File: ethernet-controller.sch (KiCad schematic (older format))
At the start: 33 parts, among them J1 5-2337992-8, U1 RTL8111H, Y1 ABM8G-25.000MHZ-18-D2Y-T

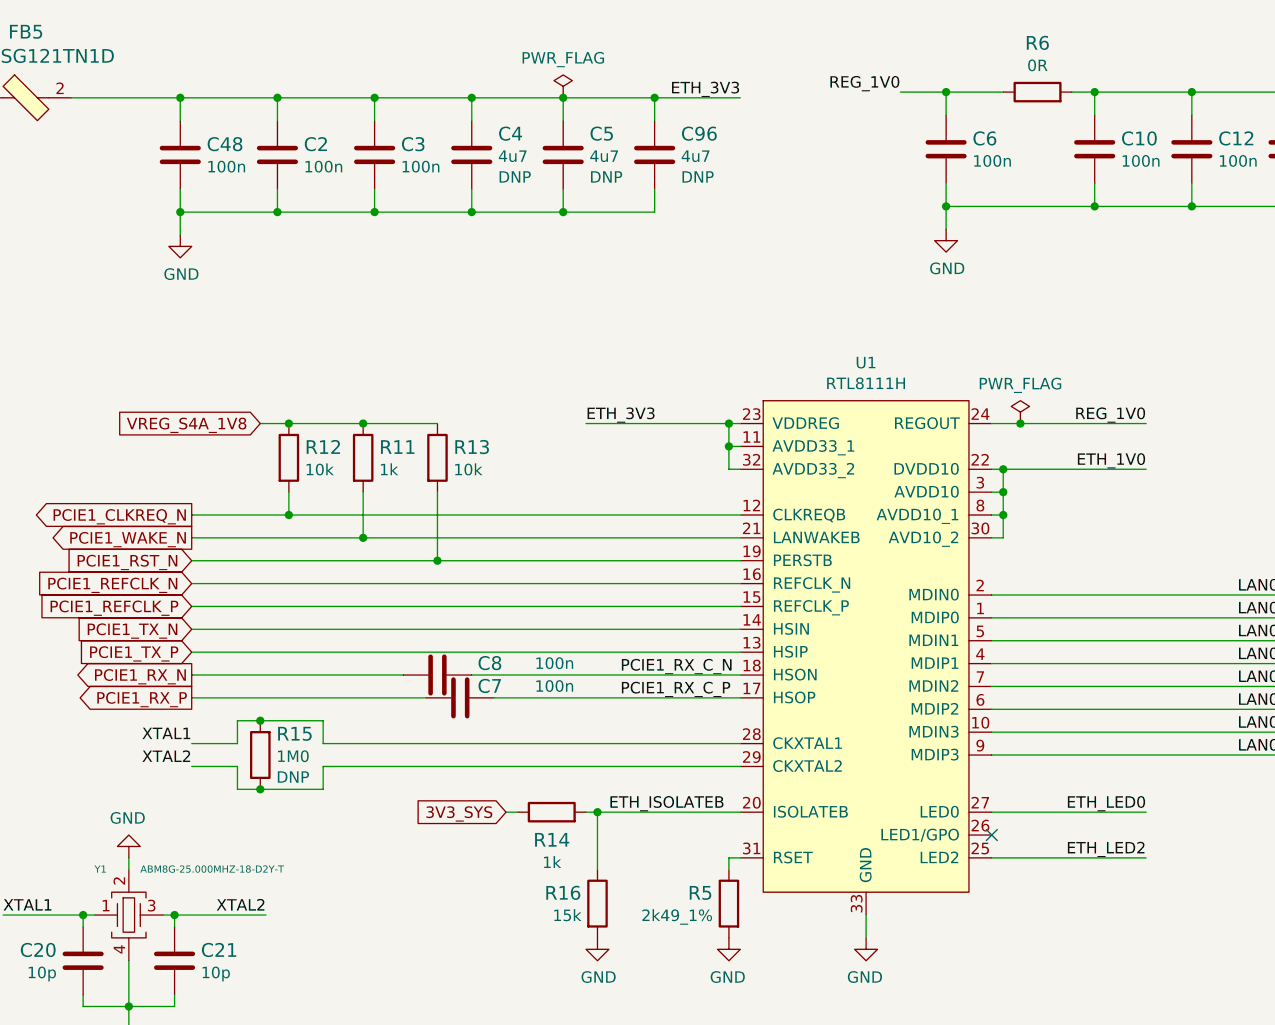
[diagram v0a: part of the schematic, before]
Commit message: Add test points
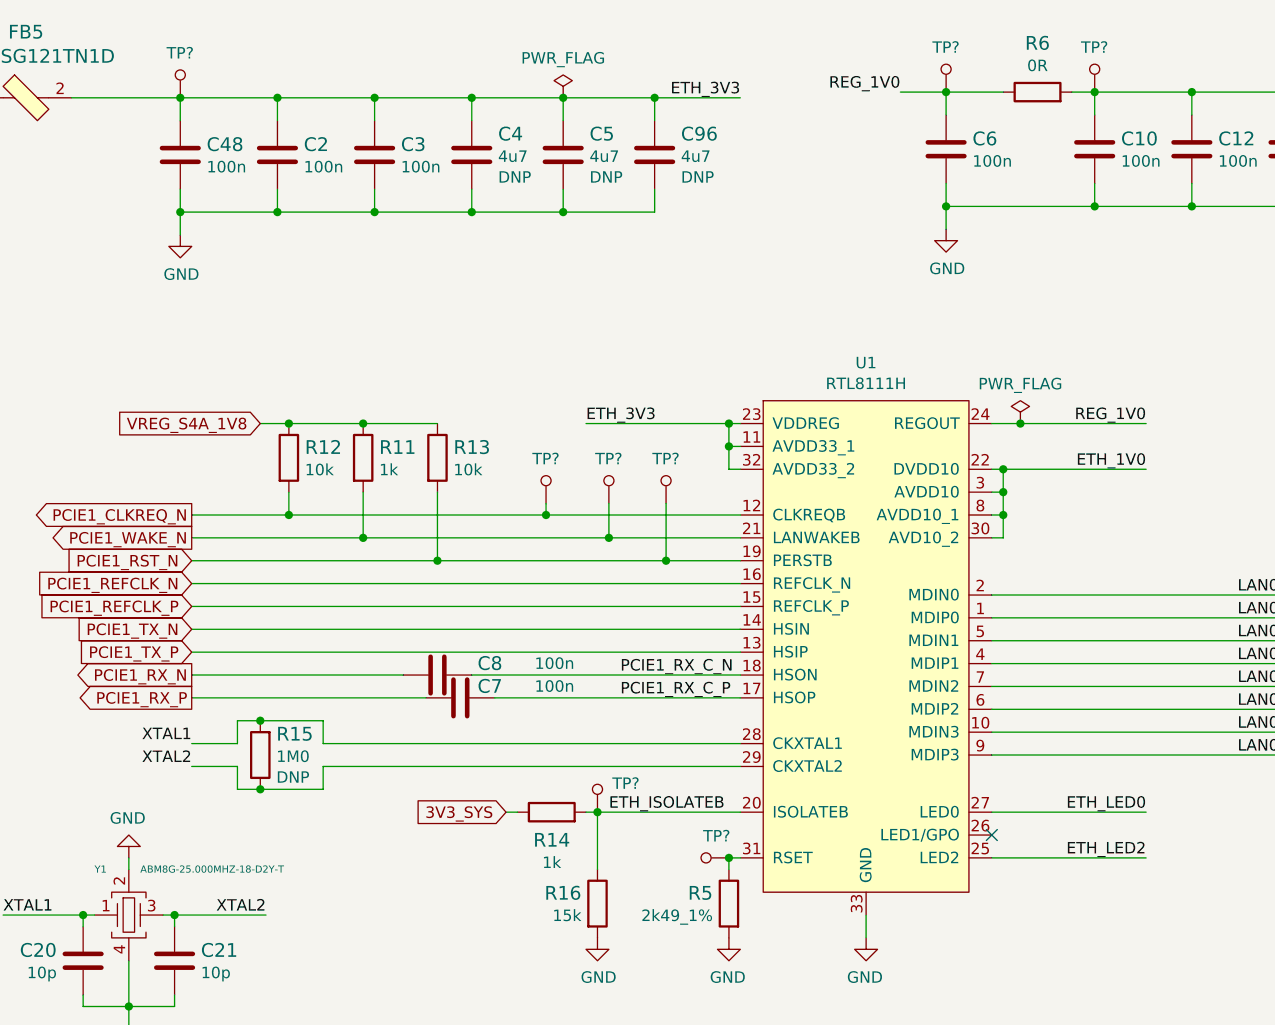
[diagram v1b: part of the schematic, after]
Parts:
- added TP? (x8): TP_SMD_0_75MM, antmicro-footprints:Testpoint_smd_0_75mm, symbol antmicroTestPoints:TP_SMD_0_75MM
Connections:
- net ETH_1V0: now also TP?.1
- net ETH_3V3: now also TP?.1
- net ETH_ISOLATEB: now also TP?.1
- net PCIE1_CLKREQ_N: now also TP?.1
- net PCIE1_RST_N: now also TP?.1
- net PCIE1_WAKE_N: now also TP?.1
- net REG_1V0: now also TP?.1
- net at R5.1, U1.31 (RSET): now also TP?.1
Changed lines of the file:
@@
 	8175 4525 8050 4525
-Wire Wire Line
-	6325 6225 6950 6225
 Wire Wire Line
 	6325 6225 6325 6475
@@
 Connection ~ 4975 4925
 Wire Wire Line
-	4975 4925 6950 4925
+	4975 4925 6100 4925
 Wire Wire Line
 	5300 4825 5300 5025
@@
 Connection ~ 5300 5025
 Wire Wire Line
-	5300 5025 6950 5025
+	5300 5025 6375 5025
 Wire Wire Line
 	5625 4825 5625 5125
 Connection ~ 5625 5125
 Wire Wire Line
-	5625 5125 6950 5125
+	5625 5125 6625 5125
 Wire Wire Line
 	4550 5225 6950 5225
@@
 Text Label 6425 5725 0    50   ~ 0
 PCIE1_RX_C_P
+$Comp
+L antmicroTestPoints:TP_SMD_0_75MM TP?
+U 1 1 624394EB
+P 4500 3000
+F 0 "TP?" H 4500 2905 50  0000 C CNN
+F 1 "TP_SMD_0_75MM" H 4500 2900 50  0001 C CNN
+F 2 "antmicro-footprints:Testpoint_smd_0_75mm" H 4700 3200 60  0001 L CNN
+F 3 "" H 4700 3300 60  0001 L CNN
+	1    4500 3000
+	-1   0    0    1
+$EndComp
+$Comp
+L antmicroTestPoints:TP_SMD_0_75MM TP?
+U 1 1 6243B4E7
+P 7850 2975
+F 0 "TP?" H 7850 2880 50  0000 C CNN
+F 1 "TP_SMD_0_75MM" H 7850 2875 50  0001 C CNN
+F 2 "antmicro-footprints:Testpoint_smd_0_75mm" H 8050 3175 60  0001 L CNN
+F 3 "" H 8050 3275 60  0001 L CNN
+	1    7850 2975
+	-1   0    0    1
+$EndComp
+$Comp
+L antmicroTestPoints:TP_SMD_0_75MM TP?
+U 1 1 62446EB7
+P 6100 4775
+F 0 "TP?" H 6100 4680 50  0000 C CNN
+F 1 "TP_SMD_0_75MM" H 6100 4675 50  0001 C CNN
+F 2 "antmicro-footprints:Testpoint_smd_0_75mm" H 6300 4975 60  0001 L CNN
+F 3 "" H 6300 5075 60  0001 L CNN
+	1    6100 4775
+	-1   0    0    1
+$EndComp
+$Comp
+L antmicroTestPoints:TP_SMD_0_75MM TP?
+U 1 1 6244F4AE
+P 6375 4775
+F 0 "TP?" H 6375 4680 50  0000 C CNN
+F 1 "TP_SMD_0_75MM" H 6375 4675 50  0001 C CNN
+F 2 "antmicro-footprints:Testpoint_smd_0_75mm" H 6575 4975 60  0001 L CNN
+F 3 "" H 6575 5075 60  0001 L CNN
+	1    6375 4775
+	-1   0    0    1
+$EndComp
+$Comp
+L antmicroTestPoints:TP_SMD_0_75MM TP?
+U 1 1 62457423
+P 6625 4775
+F 0 "TP?" H 6625 4680 50  0000 C CNN
+F 1 "TP_SMD_0_75MM" H 6625 4675 50  0001 C CNN
+F 2 "antmicro-footprints:Testpoint_smd_0_75mm" H 6825 4975 60  0001 L CNN
+F 3 "" H 6825 5075 60  0001 L CNN
+	1    6625 4775
+	-1   0    0    1
+$EndComp
+Wire Wire Line
+	6100 4875 6100 4925
+Connection ~ 6100 4925
+Wire Wire Line
+	6100 4925 6950 4925
+Wire Wire Line
+	6375 4875 6375 5025
+Connection ~ 6375 5025
+Wire Wire Line
+	6375 5025 6950 5025
+Wire Wire Line
+	6625 4875 6625 5125
+Connection ~ 6625 5125
+Wire Wire Line
+	6625 5125 6950 5125
+$Comp
+L antmicroTestPoints:TP_SMD_0_75MM TP?
+U 1 1 6247C502
+P 6325 6125
+F 0 "TP?" H 6200 6100 50  0000 C CNN
+F 1 "TP_SMD_0_75MM" H 6325 6025 50  0001 C CNN
+F 2 "antmicro-footprints:Testpoint_smd_0_75mm" H 6525 6325 60  0001 L CNN
+F 3 "" H 6525 6425 60  0001 L CNN
+	1    6325 6125
+	-1   0    0    1
+$EndComp
+Wire Wire Line
+	6325 6225 6950 6225
+$Comp
+L antmicroTestPoints:TP_SMD_0_75MM TP?
+U 1 1 6249C84E
+P 6800 6425
+F 0 "TP?" V 6705 6472 50  0000 C CNN
+F 1 "TP_SMD_0_75MM" H 6800 6325 50  0001 C CNN
+F 2 "antmicro-footprints:Testpoint_smd_0_75mm" H 7000 6625 60  0001 L CNN
+F 3 "" H 7000 6725 60  0001 L CNN
+	1    6800 6425
+	0    1    1    0
+$EndComp
+Connection ~ 6900 6425
+$Comp
+L antmicroTestPoints:TP_SMD_0_75MM TP?
+U 1 1 624AD4ED
+P 8500 2975
+F 0 "TP?" H 8500 2880 50  0000 C CNN
+F 1 "TP_SMD_0_75MM" H 8500 2875 50  0001 C CNN
+F 2 "antmicro-footprints:Testpoint_smd_0_75mm" H 8700 3175 60  0001 L CNN
+F 3 "" H 8700 3275 60  0001 L CNN
+	1    8500 2975
+	-1   0    0    1
+$EndComp
 $EndSCHEMATC

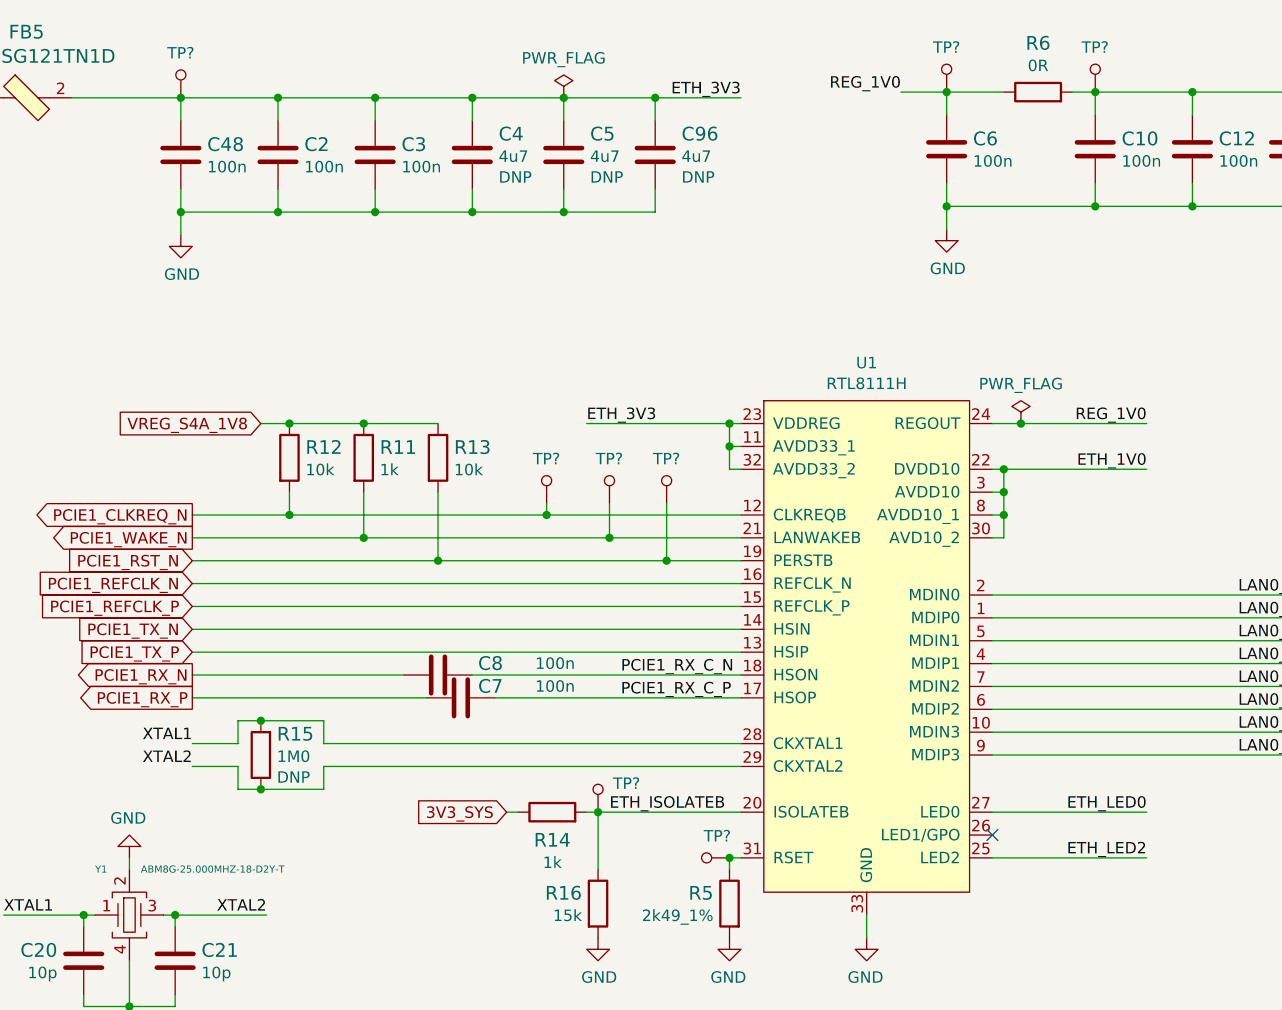
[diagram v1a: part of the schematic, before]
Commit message: Annotate test points, reimport 510R from global library
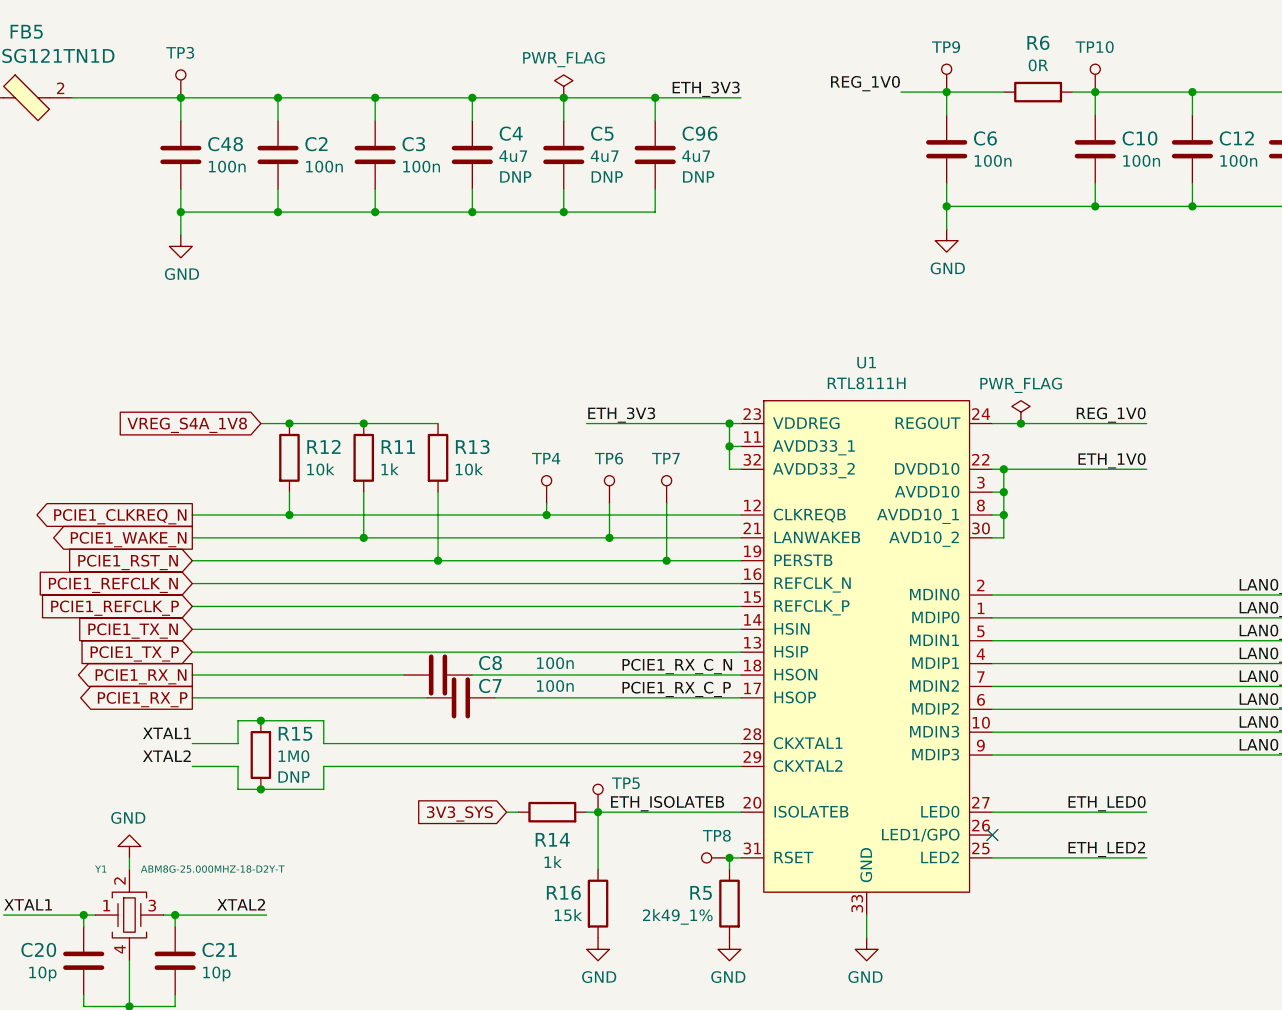
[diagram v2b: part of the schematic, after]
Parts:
- gave numbers to parts that had none: 8
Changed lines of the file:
@@
 PCIE1_RX_C_P
 $Comp
-L antmicroTestPoints:TP_SMD_0_75MM TP?
+L antmicroTestPoints:TP_SMD_0_75MM TP3
 U 1 1 624394EB
 P 4500 3000
-F 0 "TP?" H 4500 2905 50  0000 C CNN
+F 0 "TP3" H 4500 2905 50  0000 C CNN
 F 1 "TP_SMD_0_75MM" H 4500 2900 50  0001 C CNN
 F 2 "antmicro-footprints:Testpoint_smd_0_75mm" H 4700 3200 60  0001 L CNN
@@
 $EndComp
 $Comp
-L antmicroTestPoints:TP_SMD_0_75MM TP?
+L antmicroTestPoints:TP_SMD_0_75MM TP9
 U 1 1 6243B4E7
 P 7850 2975
-F 0 "TP?" H 7850 2880 50  0000 C CNN
+F 0 "TP9" H 7850 2880 50  0000 C CNN
 F 1 "TP_SMD_0_75MM" H 7850 2875 50  0001 C CNN
 F 2 "antmicro-footprints:Testpoint_smd_0_75mm" H 8050 3175 60  0001 L CNN
@@
 $EndComp
 $Comp
-L antmicroTestPoints:TP_SMD_0_75MM TP?
+L antmicroTestPoints:TP_SMD_0_75MM TP4
 U 1 1 62446EB7
 P 6100 4775
-F 0 "TP?" H 6100 4680 50  0000 C CNN
+F 0 "TP4" H 6100 4680 50  0000 C CNN
 F 1 "TP_SMD_0_75MM" H 6100 4675 50  0001 C CNN
 F 2 "antmicro-footprints:Testpoint_smd_0_75mm" H 6300 4975 60  0001 L CNN
@@
 $EndComp
 $Comp
-L antmicroTestPoints:TP_SMD_0_75MM TP?
+L antmicroTestPoints:TP_SMD_0_75MM TP6
 U 1 1 6244F4AE
 P 6375 4775
-F 0 "TP?" H 6375 4680 50  0000 C CNN
+F 0 "TP6" H 6375 4680 50  0000 C CNN
 F 1 "TP_SMD_0_75MM" H 6375 4675 50  0001 C CNN
 F 2 "antmicro-footprints:Testpoint_smd_0_75mm" H 6575 4975 60  0001 L CNN
@@
 $EndComp
 $Comp
-L antmicroTestPoints:TP_SMD_0_75MM TP?
+L antmicroTestPoints:TP_SMD_0_75MM TP7
 U 1 1 62457423
 P 6625 4775
-F 0 "TP?" H 6625 4680 50  0000 C CNN
+F 0 "TP7" H 6625 4680 50  0000 C CNN
 F 1 "TP_SMD_0_75MM" H 6625 4675 50  0001 C CNN
 F 2 "antmicro-footprints:Testpoint_smd_0_75mm" H 6825 4975 60  0001 L CNN
@@
 	6625 5125 6950 5125
 $Comp
-L antmicroTestPoints:TP_SMD_0_75MM TP?
+L antmicroTestPoints:TP_SMD_0_75MM TP5
 U 1 1 6247C502
 P 6325 6125
-F 0 "TP?" H 6200 6100 50  0000 C CNN
+F 0 "TP5" H 6200 6100 50  0000 C CNN
 F 1 "TP_SMD_0_75MM" H 6325 6025 50  0001 C CNN
 F 2 "antmicro-footprints:Testpoint_smd_0_75mm" H 6525 6325 60  0001 L CNN
@@
 	6325 6225 6950 6225
 $Comp
-L antmicroTestPoints:TP_SMD_0_75MM TP?
+L antmicroTestPoints:TP_SMD_0_75MM TP8
 U 1 1 6249C84E
 P 6800 6425
-F 0 "TP?" V 6705 6472 50  0000 C CNN
+F 0 "TP8" V 6705 6472 50  0000 C CNN
 F 1 "TP_SMD_0_75MM" H 6800 6325 50  0001 C CNN
 F 2 "antmicro-footprints:Testpoint_smd_0_75mm" H 7000 6625 60  0001 L CNN
@@
 Connection ~ 6900 6425
 $Comp
-L antmicroTestPoints:TP_SMD_0_75MM TP?
+L antmicroTestPoints:TP_SMD_0_75MM TP10
 U 1 1 624AD4ED
 P 8500 2975
-F 0 "TP?" H 8500 2880 50  0000 C CNN
+F 0 "TP10" H 8500 2880 50  0000 C CNN
 F 1 "TP_SMD_0_75MM" H 8500 2875 50  0001 C CNN
 F 2 "antmicro-footprints:Testpoint_smd_0_75mm" H 8700 3175 60  0001 L CNN

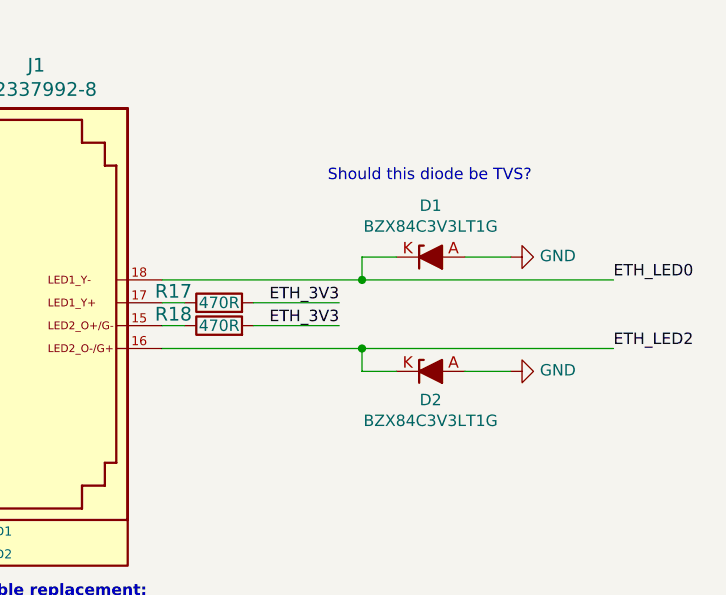
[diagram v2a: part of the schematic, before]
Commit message: Remove diodes on eth leds
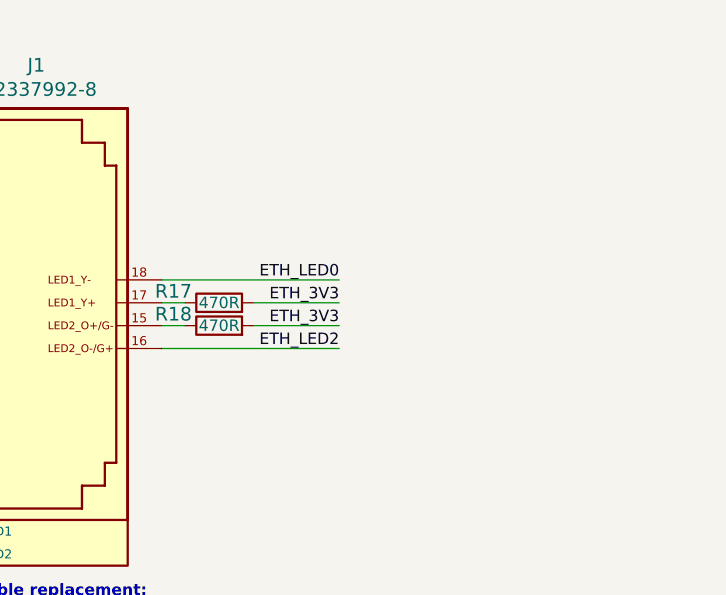
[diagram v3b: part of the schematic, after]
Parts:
- removed D1, D2: BZX84C3V3LT1G, sa800u-baseboard-hw-footprints:SOT-23-3, symbol sa800u-baseboard-hw:BZX84C3V3LT1G
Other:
- note removed: "Should this diode be TVS?"
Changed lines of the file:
@@
 LAN0_MDI0_P
-$Comp
-L sa800u-baseboard-hw:GND #PWR012
-U 1 1 61C7BF66
-P 13125 6225
-F 0 "#PWR012" H 13125 5975 50  0001 C CNN
-F 1 "GND" V 13130 6097 50  0000 R CNN
-F 2 "" H 13125 6225 50  0001 C CNN
-F 3 "" H 13125 6225 50  0001 C CNN
-	1    13125 6225
-	0    -1   -1   0
-$EndComp
-$Comp
-L sa800u-baseboard-hw:GND #PWR011
-U 1 1 61C7BBCB
-P 13125 5725
-F 0 "#PWR011" H 13125 5475 50  0001 C CNN
-F 1 "GND" V 13130 5597 50  0000 R CNN
-F 2 "" H 13125 5725 50  0001 C CNN
-F 3 "" H 13125 5725 50  0001 C CNN
-	1    13125 5725
-	0    -1   -1   0
-$EndComp
 $Comp
 L sa800u-baseboard-hw:R_470R_0402 R18
@@
 Wire Wire Line
 	11600 5925 11700 5925
-Text Label 13575 5825 0    50   ~ 0
+Text Label 12375 5825 2    50   ~ 0
 ETH_LED0
 Wire Wire Line
 	11700 6025 11600 6025
-Wire Wire Line
-	12475 6225 12475 6125
-Wire Wire Line
-	12475 5725 12475 5825
-Wire Wire Line
-	12475 5825 13575 5825
-Wire Wire Line
-	11600 5825 12475 5825
-Text Label 13575 6125 0    50   ~ 0
+Text Label 12375 6125 2    50   ~ 0
 ETH_LED2
 $Comp
@@
 Wire Wire Line
 	10050 6425 10500 6425
-$Comp
-L sa800u-baseboard-hw:BZX84C3V3LT1G D1
-U 1 1 61D774AD
-P 12775 5725
-F 0 "D1" H 12775 5950 50  0000 C CNN
-F 1 "BZX84C3V3LT1G" H 12775 5859 50  0000 C CNN
-F 2 "sa800u-baseboard-hw-footprints:SOT-23-3" H 12775 5725 50  0001 C CNN
-F 3 "https://www.farnell.com/datasheets/2236792.pdf" H 12775 5725 50  0001 C CNN
-F 4 "BZX84C3V3LT1G" H 12775 5725 50  0001 C CNN "MPN"
-F 5 "ONSEMI" H 12775 5725 50  0001 C CNN "Manufacturer"
-	1    12775 5725
-	1    0    0    -1
-$EndComp
-$Comp
-L sa800u-baseboard-hw:BZX84C3V3LT1G D2
-U 1 1 61D77E1B
-P 12775 6225
-F 0 "D2" H 12775 6100 50  0000 C CNN
-F 1 "BZX84C3V3LT1G" H 12775 6009 50  0000 C CNN
-F 2 "sa800u-baseboard-hw-footprints:SOT-23-3" H 12775 6225 50  0001 C CNN
-F 3 "https://www.farnell.com/datasheets/2236792.pdf" H 12775 6225 50  0001 C CNN
-F 4 "BZX84C3V3LT1G" H 12775 6225 50  0001 C CNN "MPN"
-F 5 "ONSEMI" H 12775 6225 50  0001 C CNN "Manufacturer"
-	1    12775 6225
-	1    0    0    -1
-$EndComp
-Wire Wire Line
-	12475 6225 12625 6225
-Wire Wire Line
-	12925 6225 13125 6225
-Wire Wire Line
-	12925 5725 13125 5725
-Wire Wire Line
-	12475 5725 12625 5725
-Text Notes 12325 5400 0    50   ~ 0
-Should this diode be TVS?
 Text Notes 10675 7300 0    50   ~ 10
 Possible replacement:\nhttps://www.l-p.com/products/457392.htm
@@
 	1    0    0    -1
 $EndComp
-Connection ~ 12475 5825
-Wire Wire Line
-	11600 6125 12475 6125
-Connection ~ 12475 6125
-Wire Wire Line
-	12475 6125 13575 6125
 $Comp
 L sa800u-baseboard-hw:C_100n_0402 C8
@@
 	-1   0    0    1
 $EndComp
+Wire Wire Line
+	11600 5825 12375 5825
+Wire Wire Line
+	11600 6125 12375 6125
 $EndSCHEMATC
